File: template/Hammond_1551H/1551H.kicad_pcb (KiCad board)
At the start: 2 copper layers, 44.5 x 29.5 mm, 2 parts

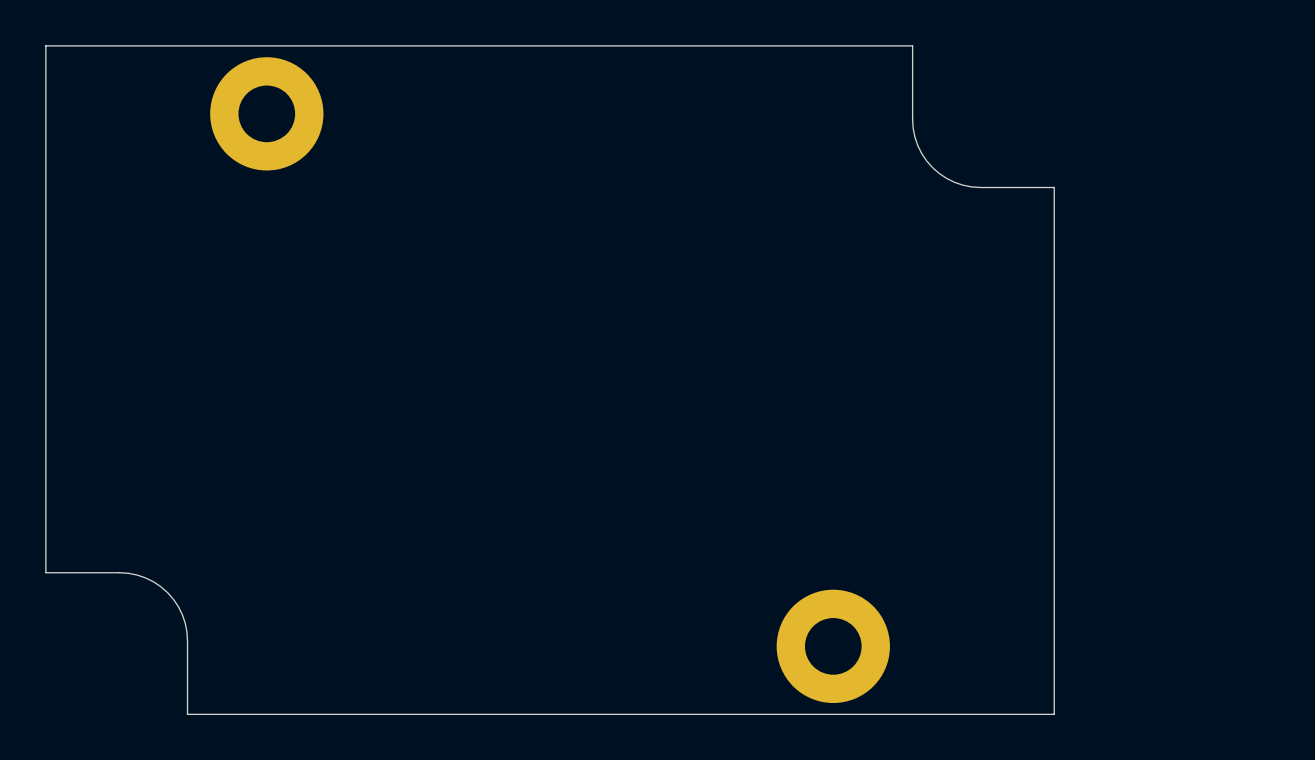
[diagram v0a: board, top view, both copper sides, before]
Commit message: feat: Add Templates for Hammond Enclosures
add templates for 1551

Issue #17
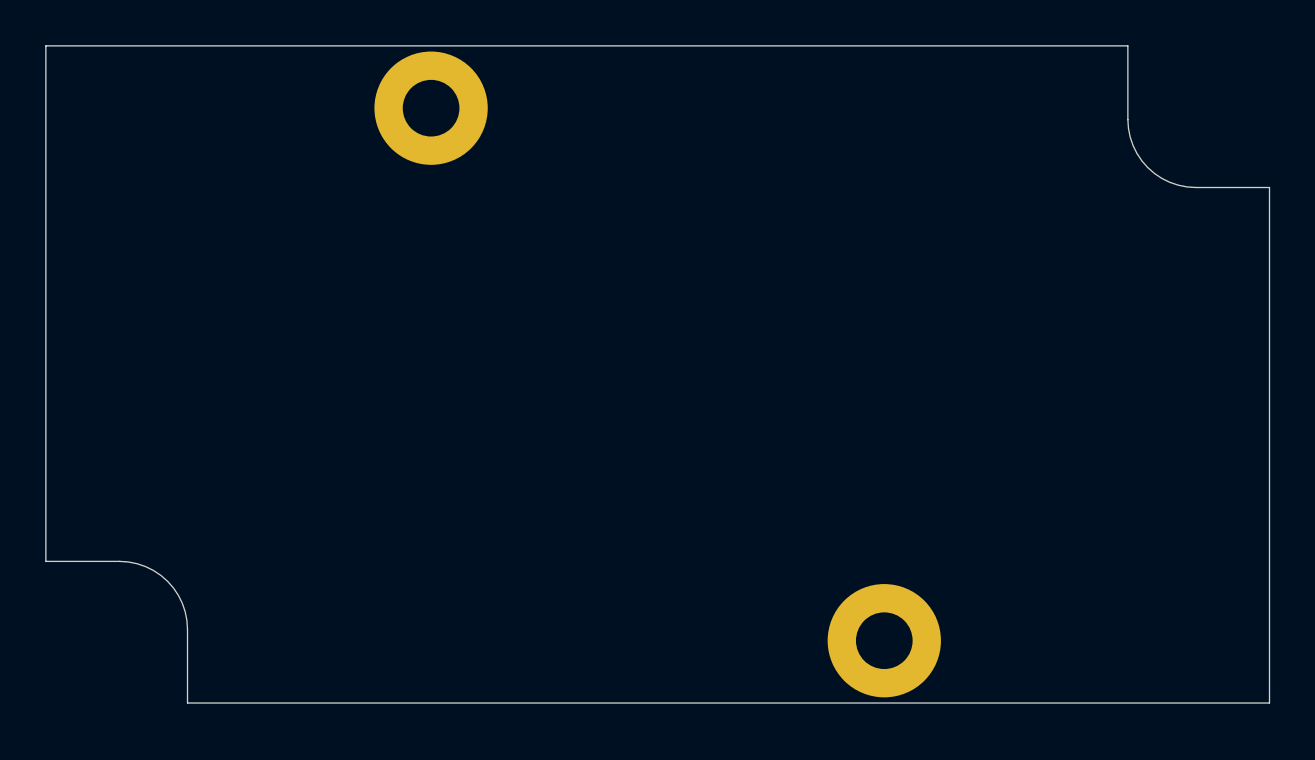
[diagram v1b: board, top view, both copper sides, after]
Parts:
- moved ~ 7.25 mm to (32.0, 17.8)
- moved ~ 2.26 mm to (52.0, 41.2)
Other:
- board size 44.5 x 29.5 mm -> 54 x 29 mm
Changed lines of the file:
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@@
     (pad_to_mask_clearance 0.051)
     (solder_mask_min_width 0.25)
-    (aux_axis_origin 15 44.5)
+    (aux_axis_origin 15 44)
     (visible_elements 7FFFFFFF)
     (pcbplotparams
@@
   )
   (module MountingHole:MountingHole_2.5mm_Pad (layer F.Cu)
-    (at 49.75 41.5)
+    (at 52 41.25)
     (descr "Mounting Hole 2.5mm")
     (tags "mounting hole 2.5mm")
@@
   )
   (module MountingHole:MountingHole_2.5mm_Pad (layer F.Cu)
-    (at 24.75 18)
+    (at 32 17.75)
     (descr "Mounting Hole 2.5mm")
     (tags "mounting hole 2.5mm")
@@
     (pad 1 thru_hole circle (at 0 0) (size 5 5) (drill 2.5) (layers *.Cu *.Mask))
   )
-  (gr_line (start 18.25 38.25) (end 15 38.25) (layer Edge.Cuts) (width 0.05))
-  (gr_line (start 21.25 44.5) (end 21.25 41.25) (layer Edge.Cuts) (width 0.05))
-  (gr_line (start 56.25 21.25) (end 59.5 21.25) (layer Edge.Cuts) (width 0.05))
-  (gr_line (start 53.25 18.25) (end 53.25 15) (layer Edge.Cuts) (width 0.05))
-  (gr_arc (start 56.25 18.25) (end 53.25 18.25) (angle -90) (layer Edge.Cuts) (width 0.05))
-  (gr_arc (start 18.25 41.25) (end 21.25 41.25) (angle -90) (layer Edge.Cuts) (width 0.05))
-  (dimension 44.5 (width 0.15) (layer Dwgs.User)
-    (gr_text "44.500 mm" (at 37.25 49.8) (layer Dwgs.User)
+  (gr_arc (start 65.75 18.25) (end 62.75 18.25) (angle -90) (layer Edge.Cuts) (width 0.05))
+  (gr_arc (start 18.25 40.75) (end 21.25 40.75) (angle -90) (layer Edge.Cuts) (width 0.05))
+  (gr_line (start 65.75 21.25) (end 69 21.25) (layer Edge.Cuts) (width 0.05))
+  (gr_line (start 62.75 15) (end 62.75 18.25) (layer Edge.Cuts) (width 0.05))
+  (gr_line (start 21.25 40.75) (end 21.25 44) (layer Edge.Cuts) (width 0.05))
+  (gr_line (start 15 37.75) (end 18.25 37.75) (layer Edge.Cuts) (width 0.05))
+  (dimension 29 (width 0.15) (layer Dwgs.User)
+    (gr_text "29,000 mm" (at 75.3 29.5 90) (layer Dwgs.User)
       (effects (font (size 1 1) (thickness 0.15)))
     )
-    (feature1 (pts (xy 15 44.5) (xy 15 49.086421)))
-    (feature2 (pts (xy 59.5 44.5) (xy 59.5 49.086421)))
-    (crossbar (pts (xy 59.5 48.5) (xy 15 48.5)))
-    (arrow1a (pts (xy 15 48.5) (xy 16.126504 47.913579)))
-    (arrow1b (pts (xy 15 48.5) (xy 16.126504 49.086421)))
-    (arrow2a (pts (xy 59.5 48.5) (xy 58.373496 47.913579)))
-    (arrow2b (pts (xy 59.5 48.5) (xy 58.373496 49.086421)))
+    (feature1 (pts (xy 69 15) (xy 74.586421 15)))
+    (feature2 (pts (xy 69 44) (xy 74.586421 44)))
+    (crossbar (pts (xy 74 44) (xy 74 15)))
+    (arrow1a (pts (xy 74 15) (xy 74.586421 16.126504)))
+    (arrow1b (pts (xy 74 15) (xy 73.413579 16.126504)))
+    (arrow2a (pts (xy 74 44) (xy 74.586421 42.873496)))
+    (arrow2b (pts (xy 74 44) (xy 73.413579 42.873496)))
   )
-  (dimension 29.5 (width 0.15) (layer Dwgs.User)
-    (gr_text "29.500 mm" (at 65.8 29.75 270) (layer Dwgs.User)
+  (dimension 54 (width 0.15) (layer Dwgs.User)
+    (gr_text "54,000 mm" (at 42 50.3) (layer Dwgs.User)
       (effects (font (size 1 1) (thickness 0.15)))
     )
-    (feature1 (pts (xy 59.5 44.5) (xy 65.086421 44.5)))
-    (feature2 (pts (xy 59.5 15) (xy 65.086421 15)))
-    (crossbar (pts (xy 64.5 15) (xy 64.5 44.5)))
-    (arrow1a (pts (xy 64.5 44.5) (xy 63.913579 43.373496)))
-    (arrow1b (pts (xy 64.5 44.5) (xy 65.086421 43.373496)))
-    (arrow2a (pts (xy 64.5 15) (xy 63.913579 16.126504)))
-    (arrow2b (pts (xy 64.5 15) (xy 65.086421 16.126504)))
+    (feature1 (pts (xy 69 44) (xy 69 49.586421)))
+    (feature2 (pts (xy 15 44) (xy 15 49.586421)))
+    (crossbar (pts (xy 15 49) (xy 69 49)))
+    (arrow1a (pts (xy 69 49) (xy 67.873496 49.586421)))
+    (arrow1b (pts (xy 69 49) (xy 67.873496 48.413579)))
+    (arrow2a (pts (xy 15 49) (xy 16.126504 49.586421)))
+    (arrow2b (pts (xy 15 49) (xy 16.126504 48.413579)))
   )
-  (gr_line (start 21.25 44.5) (end 59.5 44.5) (layer Edge.Cuts) (width 0.05))
-  (gr_line (start 59.5 21.25) (end 59.5 44.5) (layer Edge.Cuts) (width 0.05))
-  (gr_line (start 15 15) (end 15 38.25) (layer Edge.Cuts) (width 0.05))
-  (gr_line (start 15 15) (end 53.25 15) (layer Edge.Cuts) (width 0.05))
+  (gr_line (start 15 37.75) (end 15 15) (layer Edge.Cuts) (width 0.05))
+  (gr_line (start 69 44) (end 21.25 44) (layer Edge.Cuts) (width 0.05))
+  (gr_line (start 69 21.25) (end 69 44) (layer Edge.Cuts) (width 0.05))
+  (gr_line (start 15 15) (end 62.75 15) (layer Edge.Cuts) (width 0.05))
 )
